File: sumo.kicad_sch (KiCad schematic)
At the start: 57 parts, among them Q1 BPW40, Q2 BPW40, SW1 SW_Push, SW2 SW_DIP_x01, SW3 SW_DIP_x01, SW4 SW_DIP_x01, SW5 SW_DIP_x01, T1 Screw_Terminal_01x04, T2 Screw_Terminal_01x05, T3 Screw_Terminal_01x04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

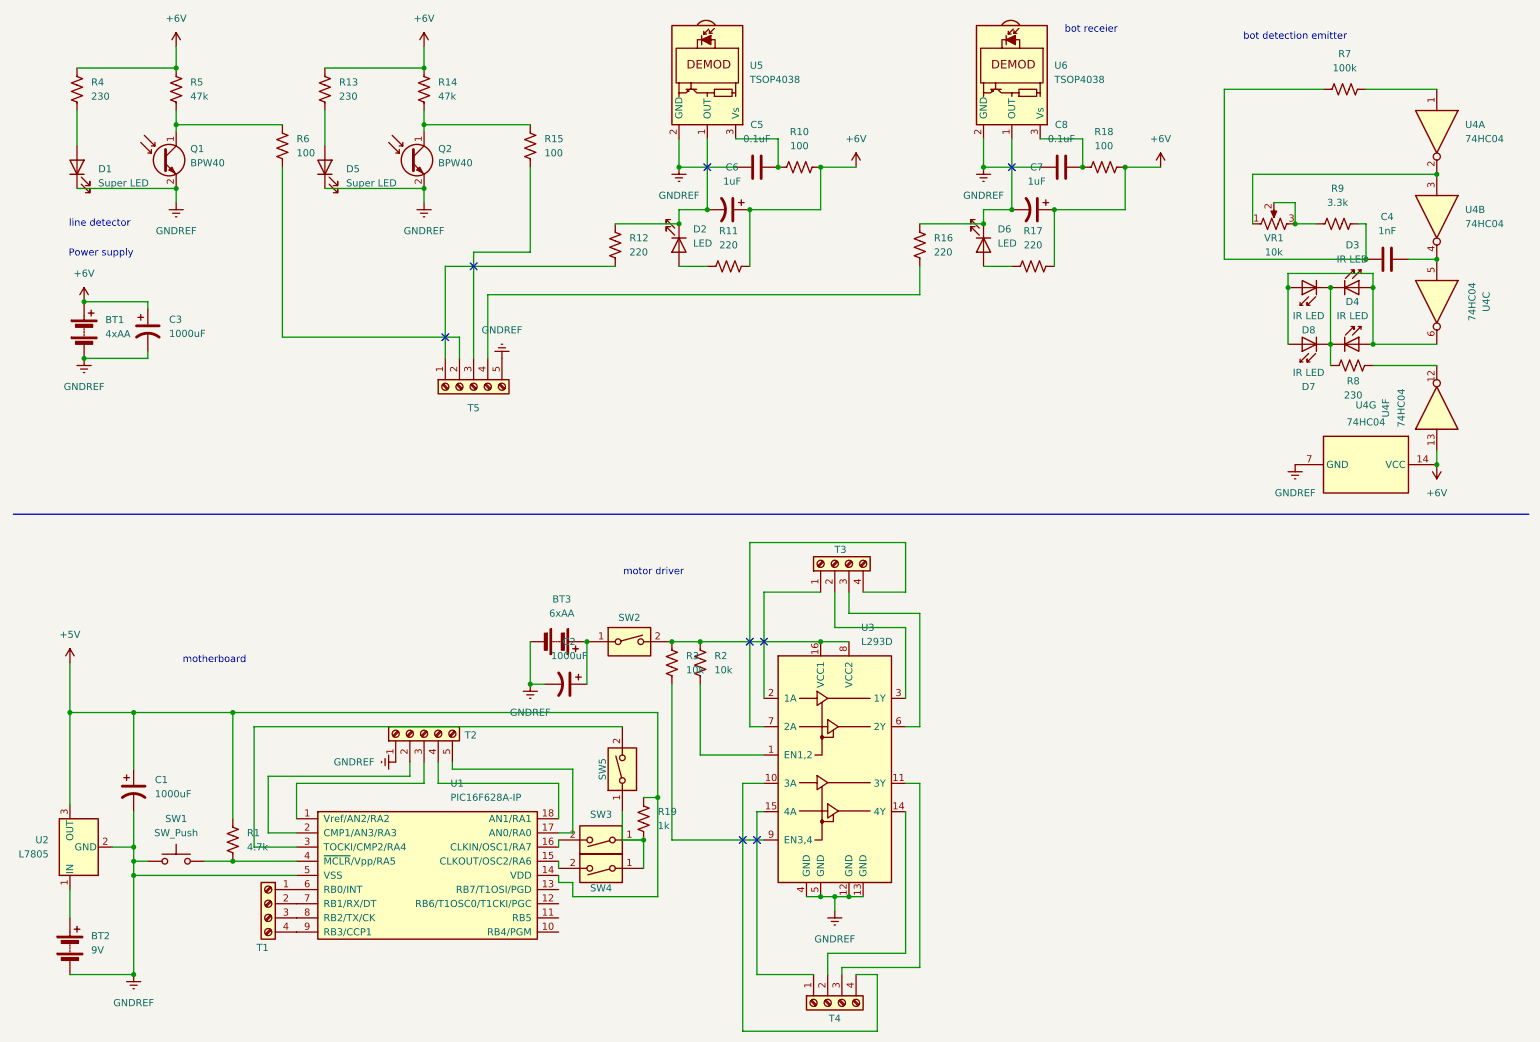
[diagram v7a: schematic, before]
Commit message: some value fixes
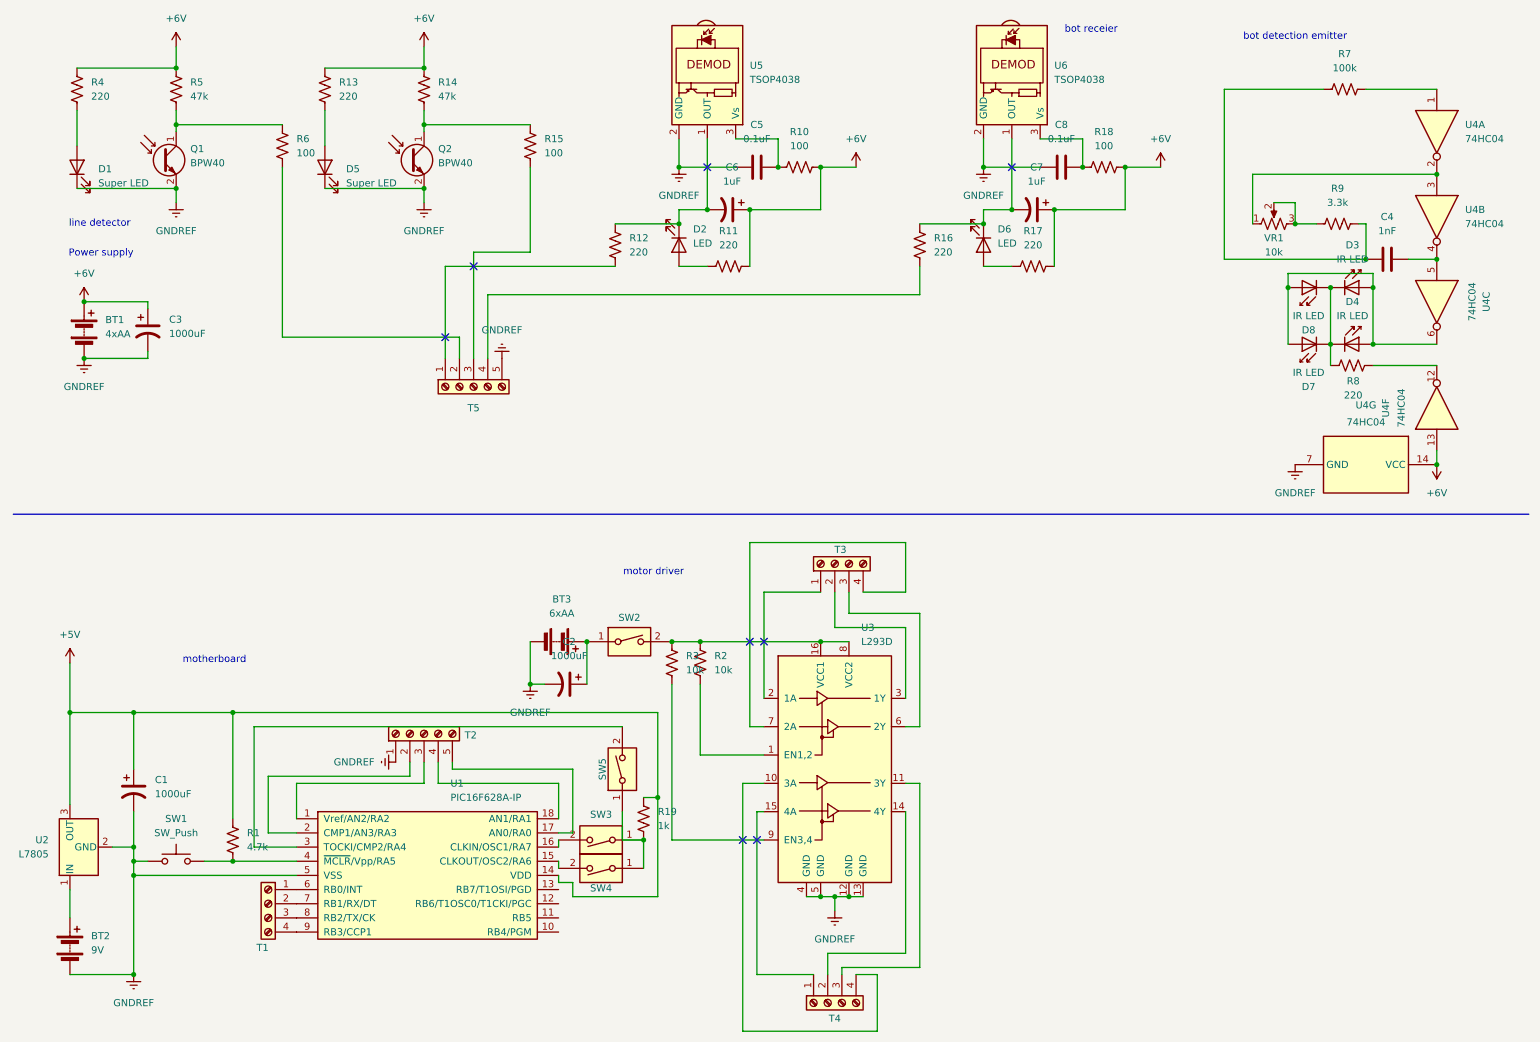
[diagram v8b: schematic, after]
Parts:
- R13, R4, R8: value 230 -> 220
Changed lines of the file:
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@@
 			)
 		)
-		(property "Value" "230"
+		(property "Value" "220"
 			(at 252.984 81.534 90)
 			(effects
@@
 			)
 		)
-		(property "Value" "230"
+		(property "Value" "220"
 			(at 26.67 27.9399 0)
 			(effects
@@
 			)
 		)
-		(property "Value" "230"
+		(property "Value" "220"
 			(at 71.12 27.9399 0)
 			(effects
